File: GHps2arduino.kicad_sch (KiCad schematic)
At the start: 20 parts, among them SW1 Green, SW2 Red, SW3 Yellow, SW4 Blue, SW5 Orange, SW6 Start, SW7 Select, SW8 Strum_Up, SW9 Strum_Down, U1 Sparkfun_Pro_Micro

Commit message: Updated With Debounce
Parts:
- added C1, C2, C3, C4, C5, C6, C7, C8, C9: 0.1uF, symbol Device:C
- added R11, R12, R13, R14, R15, R16, R17, R18, R19: 1k, symbol Device:R
- added R21, R22, R23, R24, R25, R26, R27, R28, R29: 10k, symbol Device:R
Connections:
- net Btn_Blue: now also R14.1
- net Btn_Green: now also R11.1
- net Btn_Orange: now also R15.1
- net Btn_Red: now also R12.1
- net Btn_Select: now also R17.1
- net Btn_Start: now also R16.1
- net Btn_Strm_Dn: now also R19.1
- net Btn_Strm_Up: now also R18.1
- net Btn_Yellow: now also R13.1
- net GND: now also U1.23 (GND), U1.3 (GND), U1.4 (GND), C1.2, C2.2, C3.2, C4.2, C5.2, C6.2, C7.2, C8.2, C9.2
- net Pot_Whammy: now also U1.17 (D18/A0)
- net at U1.10 (D7): now also C6.1, R16.2, R26.1
- net at U1.11 (D8/A8): now also C7.1, R17.2, R27.1
- net at U1.12 (~D9/A9): now also C8.1, R18.2, R28.1
- net at U1.13 (~D10/A10): now also C9.1, R19.2, R29.1
- net VCC: now reaches U1.21 (VCC)
- net VCC: now also R21.2, R22.2, R23.2, R24.2, R25.2, R26.2, R27.2, R28.2, R29.2
- net at U1.5 (D2): now also C1.1, R11.2, R21.1
- net at U1.6 (~D3): now also C2.1, R12.2, R22.1
- net at U1.7 (D4/A6): now also C3.1, R13.2, R23.1
- net at U1.8 (~D5): now also C4.1, R14.2, R24.1
- net at U1.9 (~D6/A7): now also C5.1, R15.2, R25.1
- no-connect marks 0 -> 10
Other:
- note added: "Usefull information - Default position for whammy is full right and fully pressed is full left - Resistance shown next to the button is the mesured value, no a physical resistance - Strum Up is D-Pad up - Strum Down is D-Pad down - Orange is Left Shoulder (LB) - Blue is X - Yellow is Y - Red is B - Green is A"
- note removed: "Usefull information - Default position for whammy is full right and fully pressed is full left - Strum Up is D-Pad up - Strum Down is D-Pad down - Orange is Left Shoulder (LB) - Blue is X - Yellow is Y - Red is B - Green is A"
- title: (none) -> Guitar Hero SG Controller to Arduino Pro Micro Conversion
- moved on the sheet: R1, R10, R2, R3, R4, R5, R6, R7, R8, R9, SW1, SW2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

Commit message: Added credits for Pro Micro library
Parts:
- U1: Credits (none) -> https://github.com/g200kg/kicad-lib-arduino
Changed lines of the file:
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@@
+			)
+		)
+		(property "Credits" "https://github.com/g200kg/kicad-lib-arduino"
+			(at 184.15 53.34 0)
+			(effects
+				(font
+					(size 1.27 1.27)
+				)
+				(hide yes)
 			)
 		)

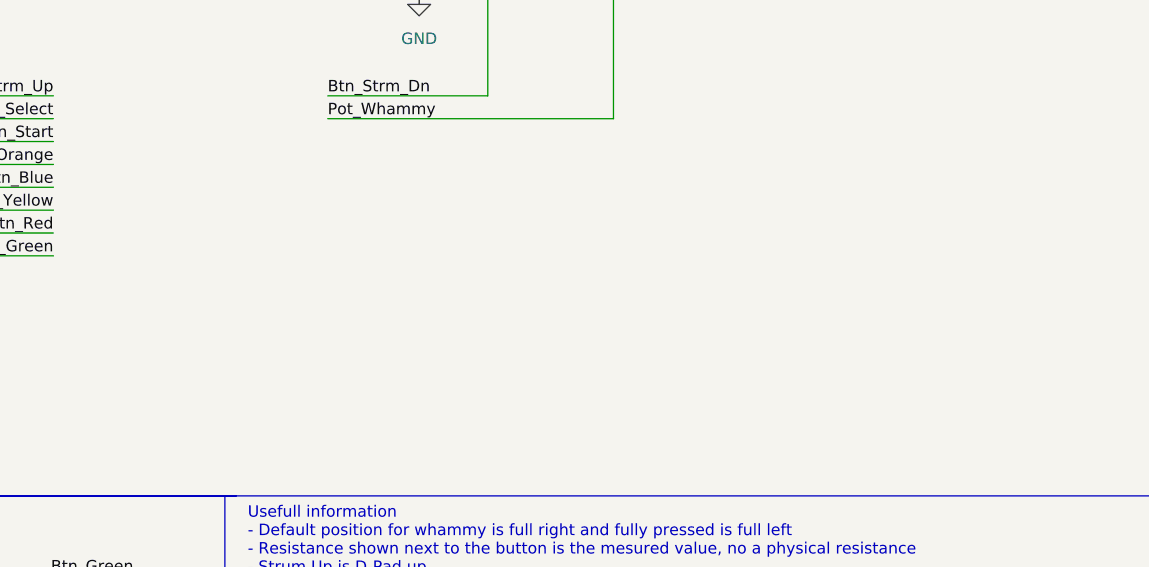
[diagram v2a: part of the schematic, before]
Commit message: Added note about missing star_power
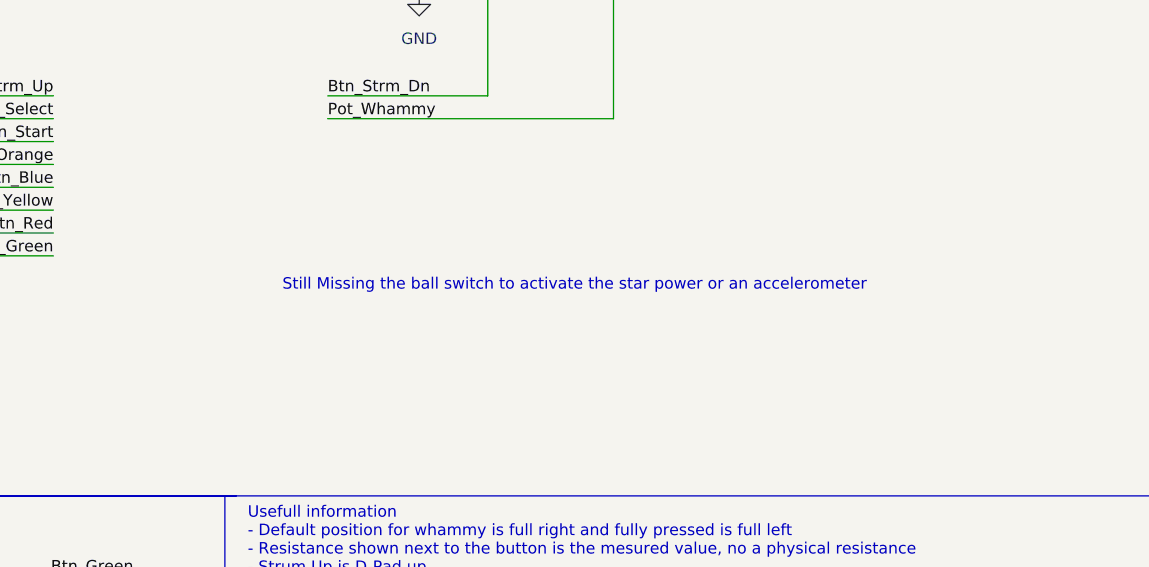
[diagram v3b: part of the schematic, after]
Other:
- note added: "Still Missing the ball switch to activate the star power or an accelerometer"
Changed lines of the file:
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@@
+		)
+	)
+	(text "Still Missing the ball switch to activate the star power or an accelerometer"
+		(exclude_from_sim no)
+		(at 215.392 120.142 0)
+		(effects
+			(font
+				(size 1.27 1.27)
+			)
 		)
 	)
